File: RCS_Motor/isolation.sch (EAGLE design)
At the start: 5 parts, among them M1 SMALL_SERVO, T1 2N2222

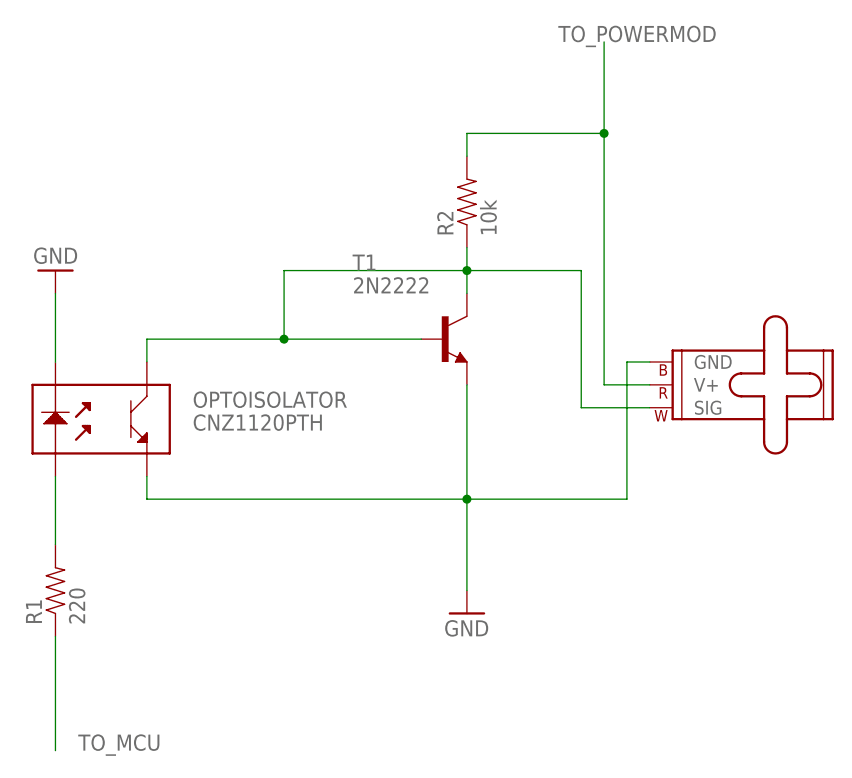
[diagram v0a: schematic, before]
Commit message: Updated/New Schematics
I don't think this updated when I did it on tuesday
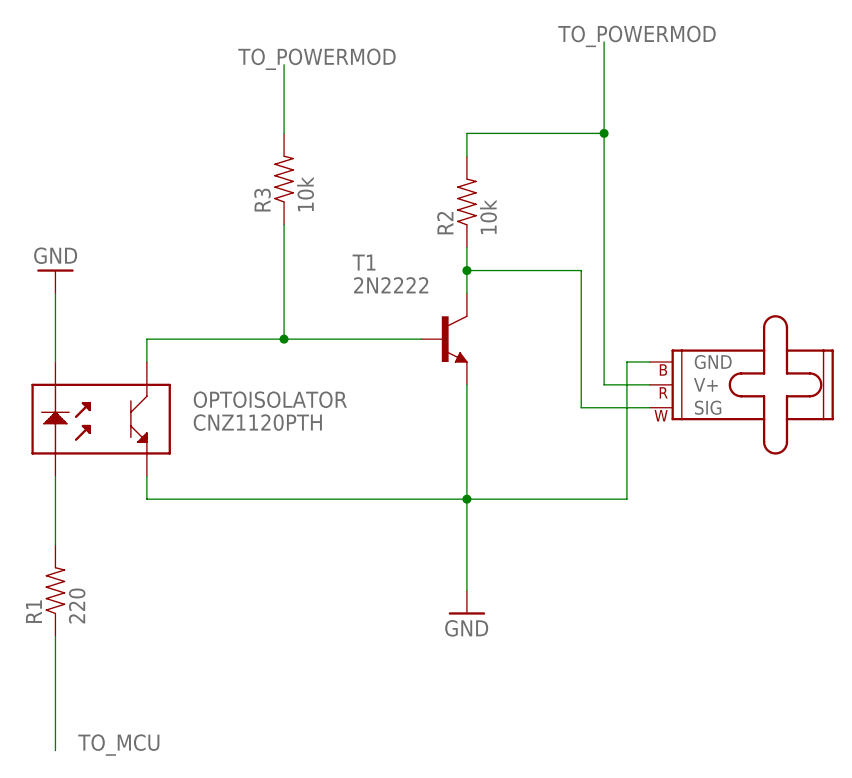
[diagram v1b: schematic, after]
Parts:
- added R3: 10k, SparkFun-Passives:RESISTOREZ
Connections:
- new net N$2: M1.SIG, R2.1, T1.C
- net N$3: now also R3.1; no longer M1.SIG, R2.1, T1.C
- net TO_POWERMOD: now also R3.2
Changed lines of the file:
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@@
 <part name="T1" library="adafruit" deviceset="2N2222" device=""/>
 <part name="GND2" library="SparkFun-Aesthetics" deviceset="GND" device=""/>
+<part name="R3" library="SparkFun-Passives" deviceset="RESISTOR" device="EZ" value="10k"/>
 </parts>
 <sheets>
@@
 <instance part="T1" gate="G$1" x="45.72" y="68.58"/>
 <instance part="GND2" gate="1" x="48.26" y="38.1"/>
+<instance part="R3" gate="G$1" x="27.94" y="86.36" rot="R90"/>
 </instances>
 <busses>
@@
 <net name="N$3" class="0">
 <segment>
-<pinref part="R2" gate="G$1" pin="1"/>
-<pinref part="T1" gate="G$1" pin="C"/>
-<wire x1="48.26" y1="78.74" x2="48.26" y2="76.2" width="0.1524" layer="91"/>
-<pinref part="M1" gate="G$1" pin="SIG"/>
-<wire x1="48.26" y1="76.2" x2="48.26" y2="73.66" width="0.1524" layer="91"/>
-<wire x1="68.58" y1="60.96" x2="60.96" y2="60.96" width="0.1524" layer="91"/>
-<wire x1="60.96" y1="60.96" x2="60.96" y2="76.2" width="0.1524" layer="91"/>
-<wire x1="60.96" y1="76.2" x2="48.26" y2="76.2" width="0.1524" layer="91"/>
-<junction x="48.26" y="76.2"/>
 <pinref part="OPTOISOLATOR" gate="G$1" pin="3"/>
 <wire x1="12.7" y1="66.04" x2="12.7" y2="68.58" width="0.1524" layer="91"/>
@@
 <pinref part="T1" gate="G$1" pin="B"/>
 <wire x1="27.94" y1="68.58" x2="43.18" y2="68.58" width="0.1524" layer="91"/>
-<wire x1="48.26" y1="76.2" x2="27.94" y2="76.2" width="0.1524" layer="91"/>
-<wire x1="27.94" y1="76.2" x2="27.94" y2="68.58" width="0.1524" layer="91"/>
+<wire x1="27.94" y1="81.28" x2="27.94" y2="68.58" width="0.1524" layer="91"/>
 <junction x="27.94" y="68.58"/>
+<pinref part="R3" gate="G$1" pin="1"/>
 </segment>
 </net>
@@
 <junction x="63.5" y="91.44"/>
 </segment>
+<segment>
+<pinref part="R3" gate="G$1" pin="2"/>
+<wire x1="27.94" y1="91.44" x2="27.94" y2="99.06" width="0.1524" layer="91"/>
+<label x="22.86" y="99.06" size="1.778" layer="95"/>
+</segment>
 </net>
+<net name="N$2" class="0">
+<segment>
+<pinref part="T1" gate="G$1" pin="C"/>
+<pinref part="R2" gate="G$1" pin="1"/>
+<wire x1="48.26" y1="78.74" x2="48.26" y2="76.2" width="0.1524" layer="91"/>
+<wire x1="48.26" y1="76.2" x2="48.26" y2="73.66" width="0.1524" layer="91"/>
+<junction x="48.26" y="76.2"/>
+<wire x1="60.96" y1="76.2" x2="48.26" y2="76.2" width="0.1524" layer="91"/>
+<pinref part="M1" gate="G$1" pin="SIG"/>
+<wire x1="68.58" y1="60.96" x2="60.96" y2="60.96" width="0.1524" layer="91"/>
+<wire x1="60.96" y1="60.96" x2="60.96" y2="76.2" width="0.1524" layer="91"/>
+</segment>
+</net>
